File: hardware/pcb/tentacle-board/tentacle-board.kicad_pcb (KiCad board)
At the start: 2 copper layers, 52 x 51 mm, 34 parts, among them J1 USB_B_Micro, J2 Conn_01x02, J3 Conn_02x18_Odd_Even, J4 Conn_02x18_Odd_Even, U1 NCP1117-3.3_SOT223, U2 W25Q128JVS, U3 RP2040, Y1 ABLS-12.000MHZ-B4-T

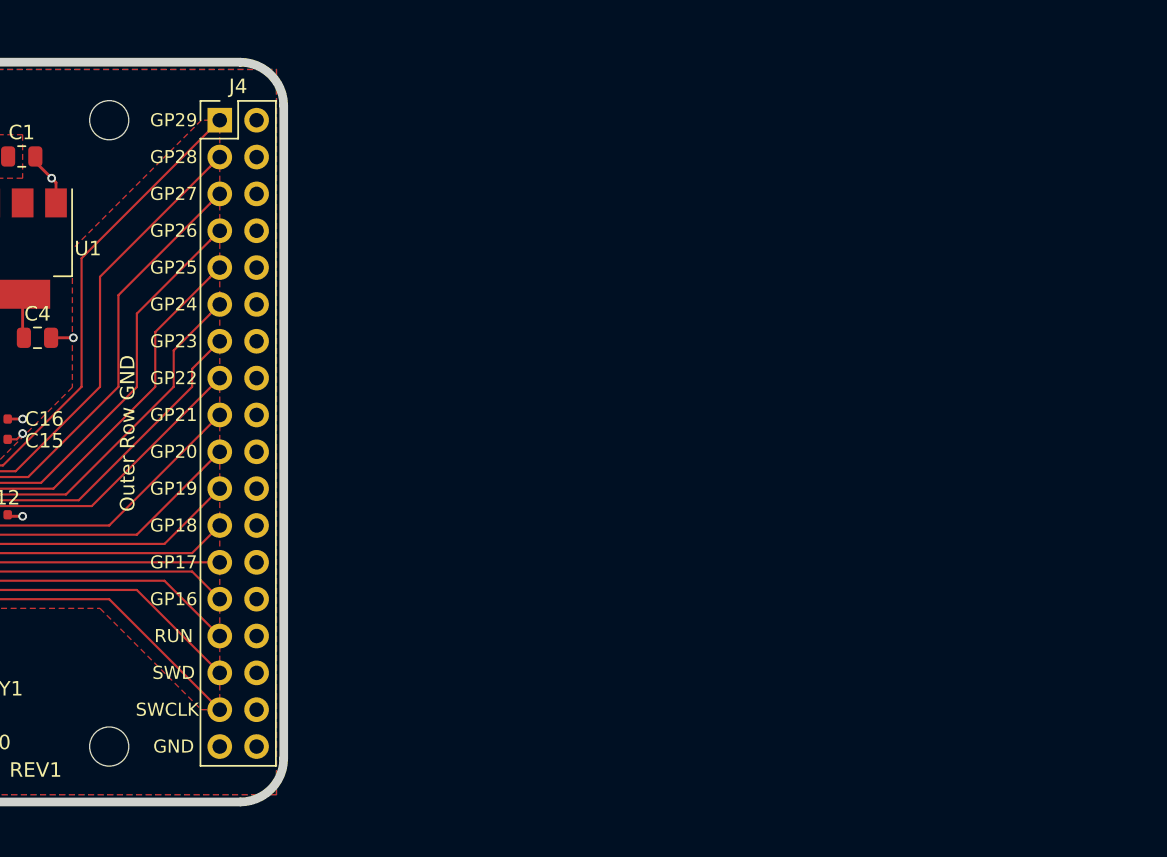
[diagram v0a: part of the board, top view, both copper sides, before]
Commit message: Added stepper drivers to the tentacle controller PCB
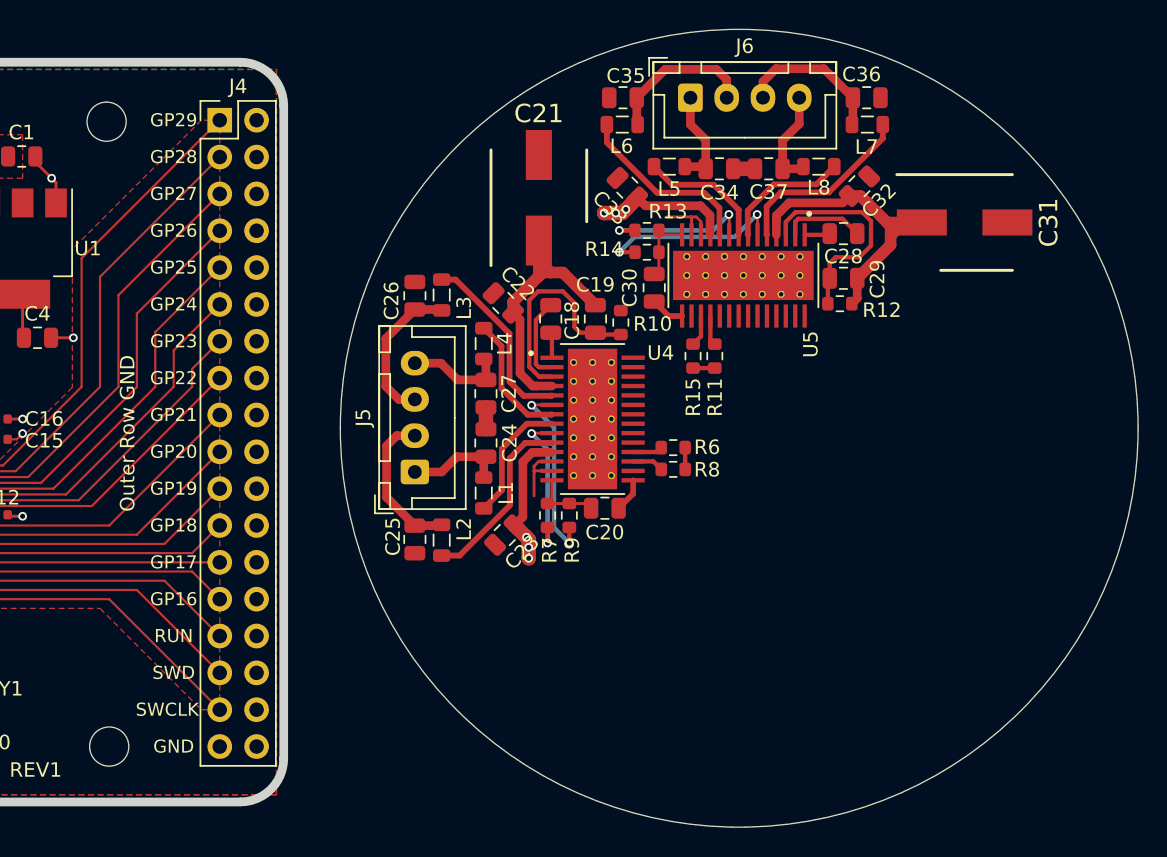
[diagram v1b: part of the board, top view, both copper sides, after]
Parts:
- added C18: 10nF, Capacitor_SMD:C_0805_2012Metric, F.Cu at (144.4, 87.7)
- added C19: 0.1uf, Capacitor_SMD:C_0805_2012Metric, F.Cu at (147.5, 87.7)
- added C20: C_Small, Capacitor_SMD:C_0805_2012Metric, F.Cu at (148.1, 100.8)
- added C21: 100uF, tentacle-board:CAPAE660X800N, F.Cu at (143.6, 79.3)
- added C22: 0.1uf, Capacitor_SMD:C_0805_2012Metric, F.Cu at (141.1, 86.6)
- added C23: 0.1uf, Capacitor_SMD:C_0805_2012Metric, F.Cu at (141.2, 102.6)
- added C24: 1n, Capacitor_SMD:C_0805_2012Metric, F.Cu at (139.9, 96.2)
- added C25: 1n, Capacitor_SMD:C_0805_2012Metric, F.Cu at (135.0, 102.9)
- added C26: 1n, Capacitor_SMD:C_0805_2012Metric, F.Cu at (135.0, 86.1)
- added C27: 1n, Capacitor_SMD:C_0805_2012Metric, F.Cu at (139.9, 92.8)
- added C28: 10nF, Capacitor_SMD:C_0805_2012Metric, F.Cu at (164.6, 81.8)
- added C29: 0.1uf, Capacitor_SMD:C_0805_2012Metric, F.Cu at (164.6, 84.9)
- added C30: C_Small, Capacitor_SMD:C_0805_2012Metric, F.Cu at (151.5, 85.5)
- added C31: 100uF, tentacle-board:CAPAE660X800N, F.Cu at (172.9, 81.0)
- added C32: 0.1uf, Capacitor_SMD:C_0805_2012Metric, F.Cu at (165.7, 78.6)
- added C33: 0.1uf, Capacitor_SMD:C_0805_2012Metric, F.Cu at (149.7, 78.6)
- added C34: 1n, Capacitor_SMD:C_0805_2012Metric, F.Cu at (156.0, 77.3)
- added C35: 1n, Capacitor_SMD:C_0805_2012Metric, F.Cu at (149.4, 72.4)
- added C36: 1n, Capacitor_SMD:C_0805_2012Metric, F.Cu at (166.2, 72.5)
- added C37: 1n, Capacitor_SMD:C_0805_2012Metric, F.Cu at (159.4, 77.3)
- added J5: Motor, Connector_JST:JST_XH_B4B-XH-A_1x04_P2.50mm_Vertical, F.Cu at (135.0, 98.2)
- added J6: Motor, Connector_JST:JST_XH_B4B-XH-A_1x04_P2.50mm_Vertical, F.Cu at (154.0, 72.4)
- added L1: L_Ferrite, Inductor_SMD:L_0805_2012Metric, F.Cu at (139.8, 99.7)
- added L2: L_Ferrite, Inductor_SMD:L_0805_2012Metric, F.Cu at (136.9, 103.0)
- added L3: L_Ferrite, Inductor_SMD:L_0805_2012Metric, F.Cu at (136.9, 86.0)
- added L4: L_Ferrite, Inductor_SMD:L_0805_2012Metric, F.Cu at (139.8, 89.4)
- added L5: L_Ferrite, Inductor_SMD:L_0805_2012Metric, F.Cu at (152.6, 77.2)
- added L6: L_Ferrite, Inductor_SMD:L_0805_2012Metric, F.Cu at (149.3, 74.3)
- added L7: L_Ferrite, Inductor_SMD:L_0805_2012Metric, F.Cu at (166.2, 74.3)
- added L8: L_Ferrite, Inductor_SMD:L_0805_2012Metric, F.Cu at (162.9, 77.2)
- added R10: R_Small, Resistor_SMD:R_0603_1608Metric, F.Cu at (149.2, 88.0)
- added R11: R_Small, Resistor_SMD:R_0603_1608Metric, F.Cu at (155.7, 90.3)
- added R12: R_Small, Resistor_SMD:R_0603_1608Metric, F.Cu at (164.3, 86.6)
- added R13: R_Small, Resistor_SMD:R_0603_1608Metric, F.Cu at (151.0, 81.6)
- added R14: R_Small, Resistor_SMD:R_0603_1608Metric, F.Cu at (151.0, 83.1)
- added R15: R_Small, Resistor_SMD:R_0603_1608Metric, F.Cu at (154.2, 90.3)
- added R6: R_Small, Resistor_SMD:R_0603_1608Metric, F.Cu at (152.9, 96.6)
- added R7: R_Small, Resistor_SMD:R_0603_1608Metric, F.Cu at (144.2, 101.2)
- added R8: R_Small, Resistor_SMD:R_0603_1608Metric, F.Cu at (152.9, 98.1)
- added R9: R_Small, Resistor_SMD:R_0603_1608Metric, F.Cu at (145.7, 101.2)
- added U4: DRV8825PWP, tentacle-board:IC_TPS61196PWPRQ1, F.Cu at (147.3, 94.6)
- added U5: DRV8825PWP, tentacle-board:IC_TPS61196PWPRQ1, F.Cu at (157.7, 84.7)
- moved H2 0.21 mm to (113.8, 74.1)
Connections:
- C1 pad 1: VBUS -> unconnected-(C1-Pad1)
- C1 pad 2: GND -> unconnected-(C1-Pad2)
- C10 pad 1: +3V3 -> unconnected-(C10-Pad1)
- C10 pad 2: GND -> unconnected-(C10-Pad2)
- C11 pad 1: +3V3 -> unconnected-(C11-Pad1)
- C11 pad 2: GND -> unconnected-(C11-Pad2)
- C12 pad 1: +3V3 -> unconnected-(C12-Pad1)
- C12 pad 2: GND -> unconnected-(C12-Pad2)
- C13 pad 1: +3V3 -> unconnected-(C13-Pad1)
- C13 pad 2: GND -> unconnected-(C13-Pad2)
- C14 pad 1: +3V3 -> unconnected-(C14-Pad1)
- C14 pad 2: GND -> unconnected-(C14-Pad2)
- C15 pad 1: +3V3 -> unconnected-(C15-Pad1)
- C15 pad 2: GND -> unconnected-(C15-Pad2)
- C16 pad 1: +3V3 -> unconnected-(C16-Pad1)
- C16 pad 2: GND -> unconnected-(C16-Pad2)
- C17 pad 1: +3V3 -> unconnected-(C17-Pad1)
- C17 pad 2: GND -> unconnected-(C17-Pad2)
- C2 pad 1: /XIN -> unconnected-(C2-Pad1)
- C2 pad 2: GND -> unconnected-(C2-Pad2)
- C3 pad 1: Net-(C3-Pad1) -> unconnected-(C3-Pad1)
- C3 pad 2: GND -> unconnected-(C3-Pad2)
- C4 pad 1: +3V3 -> unconnected-(C4-Pad1)
- C4 pad 2: GND -> unconnected-(C4-Pad2)
- C5 pad 1: +3V3 -> unconnected-(C5-Pad1)
- C5 pad 2: GND -> unconnected-(C5-Pad2)
- C6 pad 1: +1V1 -> unconnected-(C6-Pad1)
- C6 pad 2: GND -> unconnected-(C6-Pad2)
- C7 pad 1: +1V1 -> unconnected-(C7-Pad1)
- C7 pad 2: GND -> unconnected-(C7-Pad2)
- C8 pad 1: +1V1 -> unconnected-(C8-Pad1)
- C8 pad 2: GND -> unconnected-(C8-Pad2)
- C9 pad 1: +3V3 -> unconnected-(C9-Pad1)
- C9 pad 2: GND -> unconnected-(C9-Pad2)
- J1 pad 4: Net-(J1-Pad4) -> unconnected-(J1-ID-Pad4)
- R5 pad 2: Net-(C3-Pad1) -> Net-(R5-Pad2)
- Y1 pad 2: Net-(C3-Pad1) -> Net-(R5-Pad2)
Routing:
- net VMM: track 0.00 -> 65.2 mm, vias 0 -> 6
- net Net-(U5-VCP): track 0.00 -> 15.2 mm
- net Net-(U4-VCP): track 0.00 -> 15.2 mm
- net Net-(U5-ISENA): track 0.00 -> 13.3 mm, vias 0 -> 2
- net Net-(U4-ISENA): track 0.00 -> 13.3 mm, vias 0 -> 2
- net Net-(U4-AOUT1): track 0.00 -> 12.9 mm
- net Net-(U5-AOUT1): track 0.00 -> 12.9 mm
- net Net-(U5-BOUT1): track 0.00 -> 12.8 mm
- net Net-(U4-BOUT1): track 0.00 -> 12.8 mm
- net Net-(U4-ISENB): track 0.00 -> 10.7 mm, vias 0 -> 2
- net Net-(U5-ISENB): track 0.00 -> 10.7 mm, vias 0 -> 2
- net /Motor Driver/B1: track 0.00 -> 10.4 mm
- net /Motor Driver1/B1: track 0.00 -> 10.4 mm
- net /Motor Driver1/A1: track 0.00 -> 10.4 mm
- net /Motor Driver/A1: track 0.00 -> 10.4 mm
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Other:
- board size 52 x 51 mm -> 110.9 x 55 mm

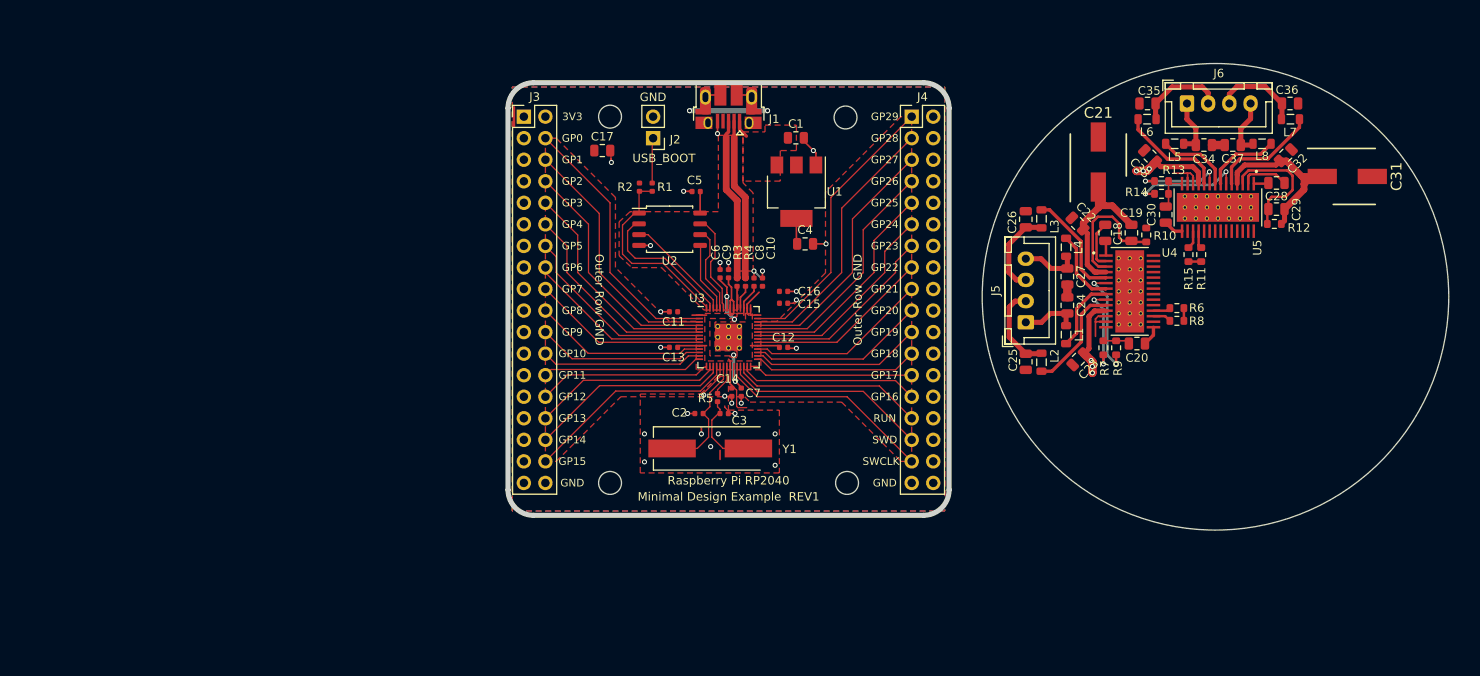
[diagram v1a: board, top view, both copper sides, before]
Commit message: Worked on the motor power system and stepper driver BOM
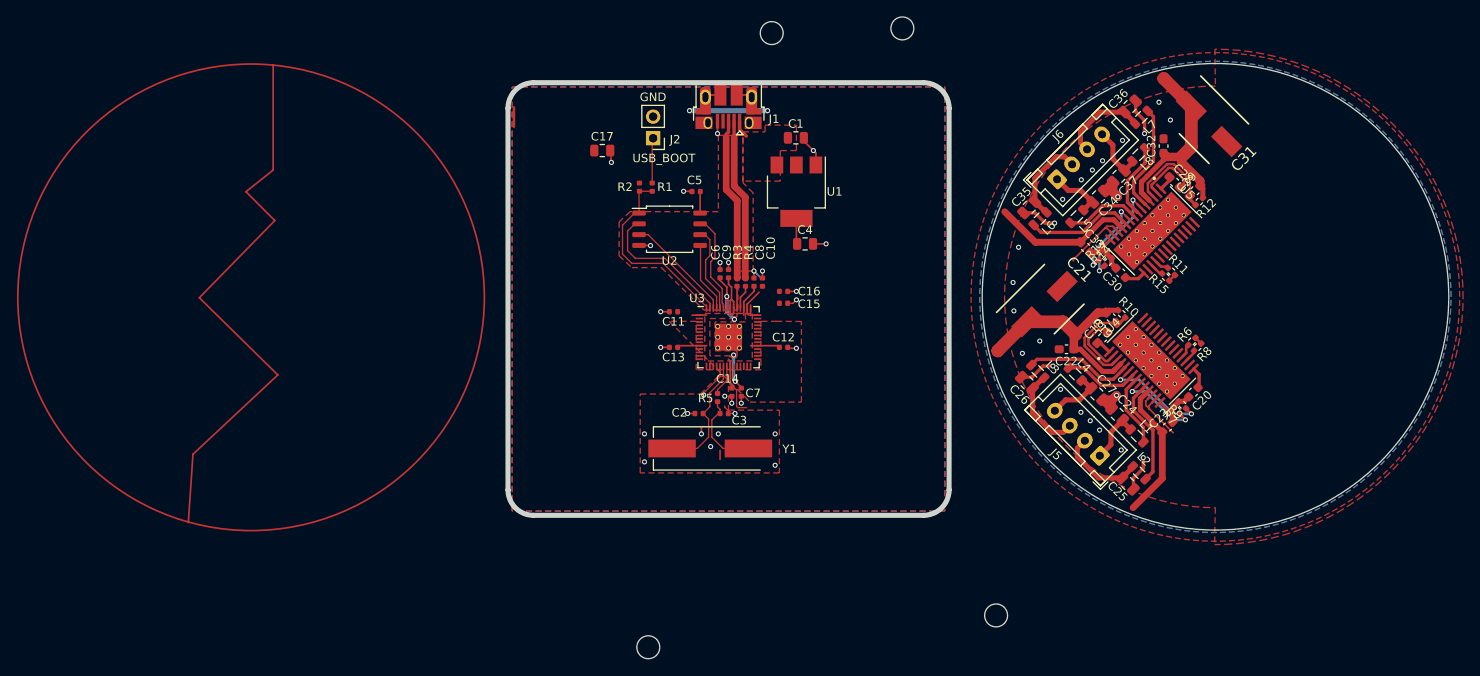
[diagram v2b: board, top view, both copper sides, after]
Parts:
- removed J3, J4: Conn_02x18_Odd_Even, Connector_PinHeader_2.54mm:PinHeader_2x18_P2.54mm_Vertical
- C18, C19, C22, C23, C28, C29, C32, C33: footprint Capacitor_SMD:C_0805_2012Metric -> Capacitor_SMD:C_0603_1608Metric_Pad1.08x0.95mm_HandSolder
- C20, C30: value C_Small -> 0.47uF; footprint Capacitor_SMD:C_0805_2012Metric -> Capacitor_SMD:C_0603_1608Metric
- C24, C25, C26, C27, C34, C35, C36, C37: value 1n -> 1nF
- R10, R12: value R_Small -> 1M; footprint Resistor_SMD:R_0603_1608Metric -> Resistor_SMD:R_0402_1005Metric_Pad0.72x0.64mm_HandSolder
- R11, R6: value R_Small -> 1.5k; footprint Resistor_SMD:R_0603_1608Metric -> Resistor_SMD:R_0402_1005Metric_Pad0.72x0.64mm_HandSolder
- R13, R14, R7, R9: value R_Small -> 0.1; footprint Resistor_SMD:R_0603_1608Metric -> Resistor_SMD:R_0402_1005Metric_Pad0.72x0.64mm_HandSolder
- R15, R8: value R_Small -> 10k; footprint Resistor_SMD:R_0603_1608Metric -> Resistor_SMD:R_0402_1005Metric_Pad0.72x0.64mm_HandSolder
- moved H3 23.5 mm to (131.5, 132.8)
- moved H1 21.5 mm to (105.1, 64.2)
- moved H4 19.9 mm to (90.5, 136.6)
- moved C26 19.3 mm to (135.2, 105.4), turned to 135 degrees
- moved C36 18.9 mm to (147.3, 72.8), turned to 45 degrees
- moved C25 18.7 mm to (147.1, 117.3), turned to -45 degrees
- moved C35 18.5 mm to (135.4, 84.7), turned to -135 degrees
- moved L3 18.0 mm to (136.5, 104.0), turned to -45 degrees
- moved J5 18.0 mm to (143.8, 114.0), turned to 135 degrees
- moved C21 17.9 mm to (137.2, 96.1), turned to 45 degrees
- moved J6 17.7 mm to (138.7, 81.4), turned to 45 degrees
- moved L7 17.6 mm to (148.7, 74.1), turned to -135 degrees
- moved C31 17.4 mm to (156.6, 74.8), turned to -45 degrees
- moved L2 17.4 mm to (148.4, 116.0), turned to 135 degrees
- moved L6 17.2 mm to (136.7, 86.0), turned to 45 degrees
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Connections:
- C1 pad 1: unconnected-(C1-Pad1) -> VBUS
- C1 pad 2: unconnected-(C1-Pad2) -> GND
- C10 pad 1: unconnected-(C10-Pad1) -> +3V3
- C10 pad 2: unconnected-(C10-Pad2) -> GND
- C11 pad 1: unconnected-(C11-Pad1) -> +3V3
- C11 pad 2: unconnected-(C11-Pad2) -> GND
- C12 pad 1: unconnected-(C12-Pad1) -> +3V3
- C12 pad 2: unconnected-(C12-Pad2) -> GND
- C13 pad 1: unconnected-(C13-Pad1) -> +3V3
- C13 pad 2: unconnected-(C13-Pad2) -> GND
- C14 pad 1: unconnected-(C14-Pad1) -> +3V3
- C15 pad 1: unconnected-(C15-Pad1) -> +3V3
- C15 pad 2: unconnected-(C15-Pad2) -> GND
- C16 pad 1: unconnected-(C16-Pad1) -> +3V3
- C16 pad 2: unconnected-(C16-Pad2) -> GND
- C17 pad 1: unconnected-(C17-Pad1) -> +3V3
- C17 pad 2: unconnected-(C17-Pad2) -> GND
- C2 pad 1: unconnected-(C2-Pad1) -> /XIN
- C2 pad 2: unconnected-(C2-Pad2) -> GND
- C3 pad 1: unconnected-(C3-Pad1) -> Net-(C3-Pad1)
- C3 pad 2: unconnected-(C3-Pad2) -> GND
- C4 pad 1: unconnected-(C4-Pad1) -> +3V3
- C4 pad 2: unconnected-(C4-Pad2) -> GND
- C5 pad 1: unconnected-(C5-Pad1) -> +3V3
- C5 pad 2: unconnected-(C5-Pad2) -> GND
- C6 pad 1: unconnected-(C6-Pad1) -> +1V1
- C6 pad 2: unconnected-(C6-Pad2) -> GND
- C7 pad 1: unconnected-(C7-Pad1) -> +1V1
- C7 pad 2: unconnected-(C7-Pad2) -> GND
- C8 pad 1: unconnected-(C8-Pad1) -> +1V1
- C8 pad 2: unconnected-(C8-Pad2) -> GND
- C9 pad 1: unconnected-(C9-Pad1) -> +3V3
- C9 pad 2: unconnected-(C9-Pad2) -> GND
- R5 pad 2: Net-(R5-Pad2) -> Net-(C3-Pad1)
- Y1 pad 2: Net-(R5-Pad2) -> Net-(C3-Pad1)
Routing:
- net GND: track 29.3 -> 77.0 mm, vias 12 -> 50
- net /GPIO29_ADC3: track 33.2 -> 0.00 mm
- net /GPIO0: track 31.8 -> 0.00 mm
- net /GPIO28_ADC2: track 31.6 -> 0.00 mm
- net /GPIO1: track 30.2 -> 0.00 mm
- net /GPIO27_ADC1: track 29.9 -> 0.00 mm
- net /GPIO2: track 28.5 -> 0.00 mm
- net /GPIO26_ADC0: track 28.3 -> 0.00 mm
- net /GPIO3: track 26.9 -> 0.00 mm
- net /GPIO25: track 26.7 -> 0.00 mm
- net /SWCLK: track 25.9 -> 0.00 mm
- net /GPIO15: track 25.4 -> 0.00 mm
- net /GPIO4: track 25.3 -> 0.00 mm
- net /GPIO24: track 25.0 -> 0.00 mm
- net /SWD: track 24.3 -> 0.00 mm
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- added copper zone on F.Cu, net VMM
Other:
- board text removed: "3V3"
- board text removed: "GP0"
- board text removed: "GP1"
- board text removed: "GP10"
- board text removed: "GP11"
- board text removed: "GP12"
- board text removed: "GP13"
- board text removed: "GP14"
- board text removed: "GP15"
- board text removed: "GP16"
- board text removed: "GP17"
- board text removed: "GP18"
- board text removed: "GP19"
- board text removed: "GP2"
- board text removed: "GP20"
- board text removed: "GP21"
- board text removed: "GP22"
- board text removed: "GP23"
- board text removed: "GP24"
- board text removed: "GP25"
- board text removed: "GP26"
- board text removed: "GP27"
- board text removed: "GP28"
- board text removed: "GP29"
- board text removed: "GP3"
- board text removed: "GP4"
- board text removed: "GP5"
- board text removed: "GP6"
- board text removed: "GP7"
- board text removed: "GP8"
- board text removed: "GP9"
- board text removed: "Minimal Design Example REV1"
- board text removed: "Outer Row GND"
- board text removed: "RUN"
- board text removed: "Raspberry Pi RP2040"
- board text removed: "SWCLK"
- board text removed: "SWD"
